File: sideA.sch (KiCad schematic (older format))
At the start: 18 parts, among them J1 USB_2, P1 CONN_2, Q1 NPN, Q2 NPN, Q3 NPN, SW1 SW_PUSH, SW2 SW_PUSH, SW3 SW_PUSH

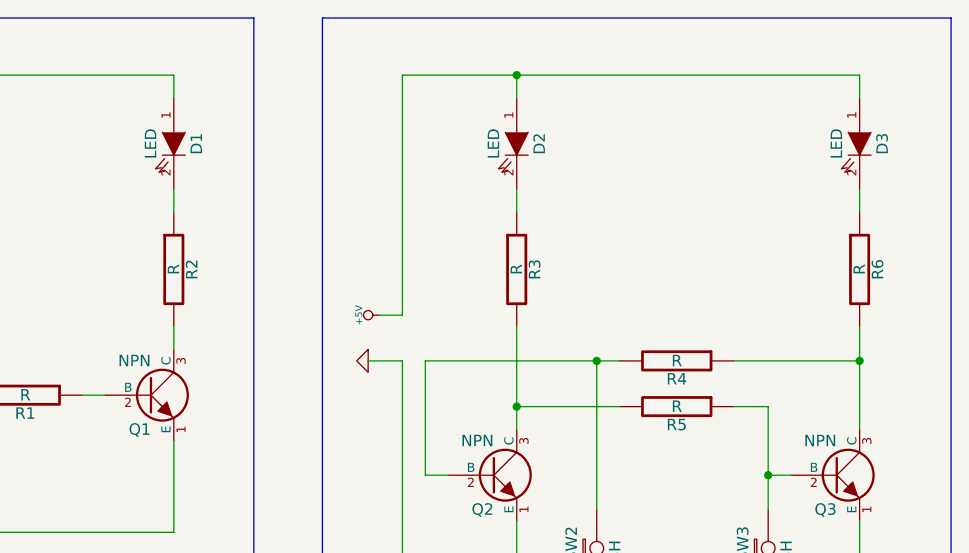
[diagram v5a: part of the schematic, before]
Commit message: LED resistors value (150ohm) added to schematics.
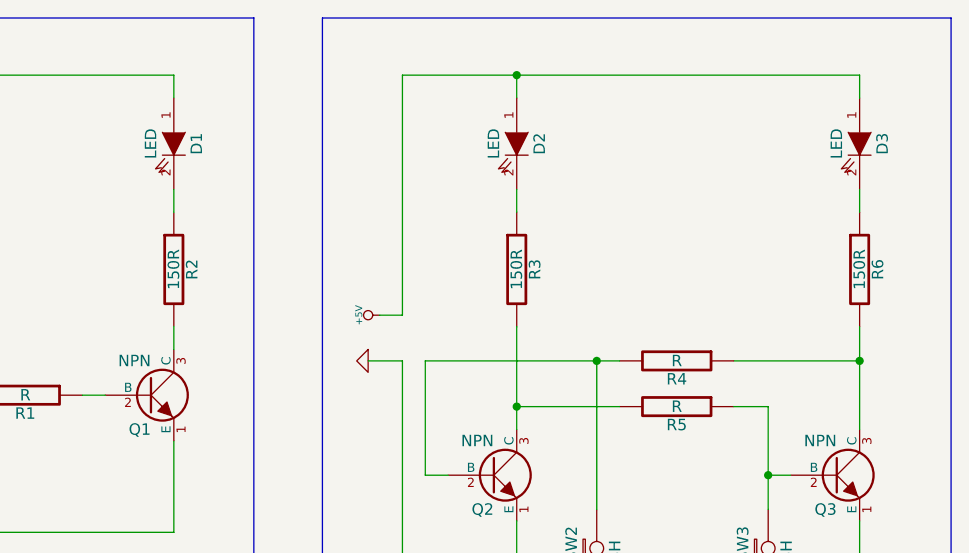
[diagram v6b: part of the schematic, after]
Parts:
- R2, R3, R6: value R -> 150R
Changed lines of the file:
@@
-EESchema Schematic File Version 2  date Tue 26 Feb 2013 22:33:32 CET
+EESchema Schematic File Version 2  date Tue 26 Feb 2013 22:56:48 CET
 LIBS:power
 LIBS:device
@@
 P 7350 2200
 F 0 "R6" V 7430 2200 50  0000 C CNN
-F 1 "R" V 7350 2200 50  0000 C CNN
+F 1 "150R" V 7350 2200 50  0000 C CNN
 	1    7350 2200
 	1    0    0    -1
@@
 P 5850 2200
 F 0 "R3" V 5930 2200 50  0000 C CNN
-F 1 "R" V 5850 2200 50  0000 C CNN
+F 1 "150R" V 5850 2200 50  0000 C CNN
 	1    5850 2200
 	1    0    0    -1
@@
 P 4350 2200
 F 0 "R2" V 4430 2200 50  0000 C CNN
-F 1 "R" V 4350 2200 50  0000 C CNN
+F 1 "150R" V 4350 2200 50  0000 C CNN
 	1    4350 2200
 	1    0    0    -1

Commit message: All components spitted on the board.
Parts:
- R1, R4, R5: value R -> 22K
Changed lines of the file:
@@
-EESchema Schematic File Version 2  date Tue 26 Feb 2013 22:56:48 CET
+EESchema Schematic File Version 2  date Wed 27 Feb 2013 15:39:57 CET
 LIBS:power
 LIBS:device
@@
 Sheet 1 1
 Title "SMT4dummies - sideA"
-Date "26 feb 2013"
+Date "27 feb 2013"
 Rev ""
 Comp "d-Squared Robotics"
@@
 P 6550 2600
 F 0 "R4" V 6630 2600 50  0000 C CNN
-F 1 "R" V 6550 2600 50  0000 C CNN
+F 1 "22K" V 6550 2600 50  0000 C CNN
 	1    6550 2600
 	0    1    1    0
@@
 P 6550 2800
 F 0 "R5" V 6630 2800 50  0000 C CNN
-F 1 "R" V 6550 2800 50  0000 C CNN
+F 1 "22K" V 6550 2800 50  0000 C CNN
 	1    6550 2800
 	0    1    1    0
@@
 P 3700 2750
 F 0 "R1" V 3780 2750 50  0000 C CNN
-F 1 "R" V 3700 2750 50  0000 C CNN
+F 1 "22K" V 3700 2750 50  0000 C CNN
 	1    3700 2750
 	0    1    1    0
